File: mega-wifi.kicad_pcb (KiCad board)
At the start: 2 copper layers, 83.8 x 51 mm, 51 parts, among them P1 NP, P2 MD-CART-FINGERS, Q1 2N7002, U1 SC16C550BIB48, U2 S29GL032N, U3 ESP-12E, U4 AZ1117CH-3.3, U5 74LVC1G08GW, U6 74LVC162245, U7 74LVC245, U8 74LVC162245, Y1 24 MHz

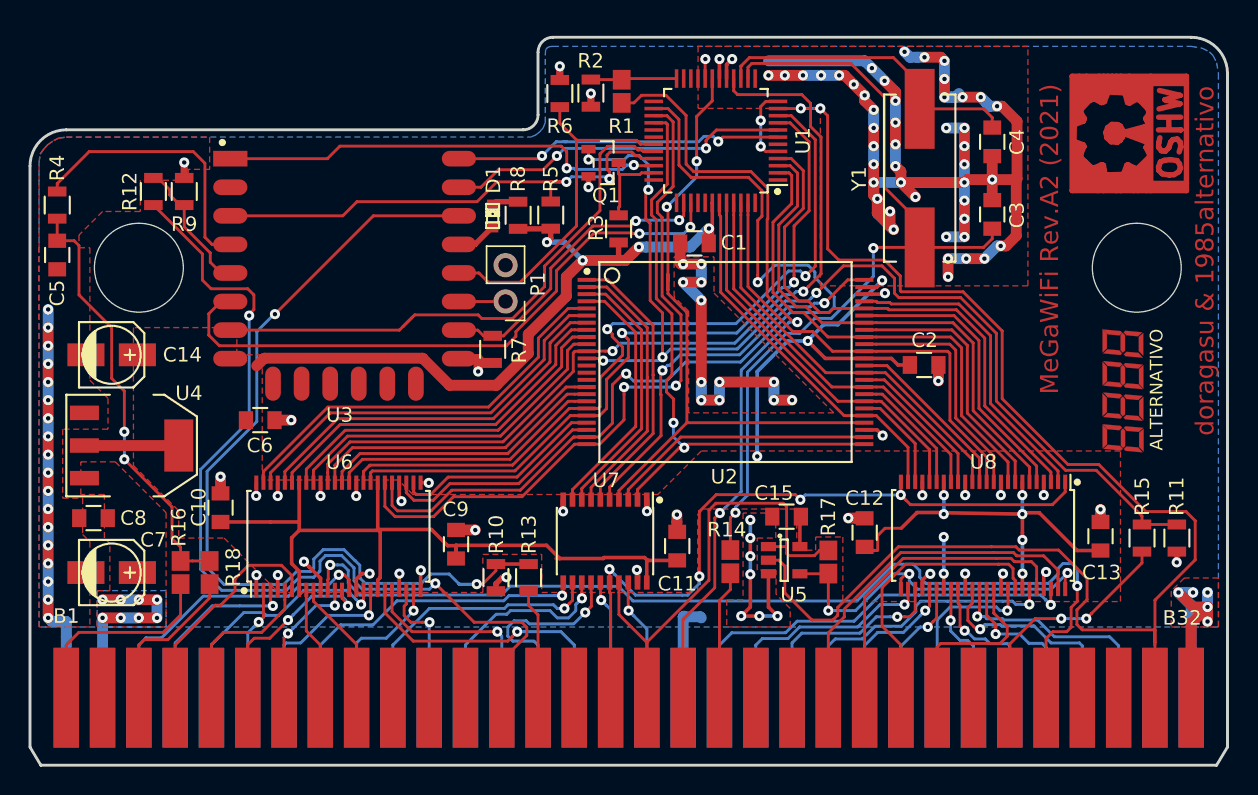
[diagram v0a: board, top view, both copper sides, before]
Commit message: Rev.B PCB
* Replace obsolete SC16C550BIB48 with SC16C550BIBS
* Replace ESP8266 with ESP32-C3
* Implement 64 Mbit hack
* Add USB-C debug header for ESP32-C3
* Many PCB improvements
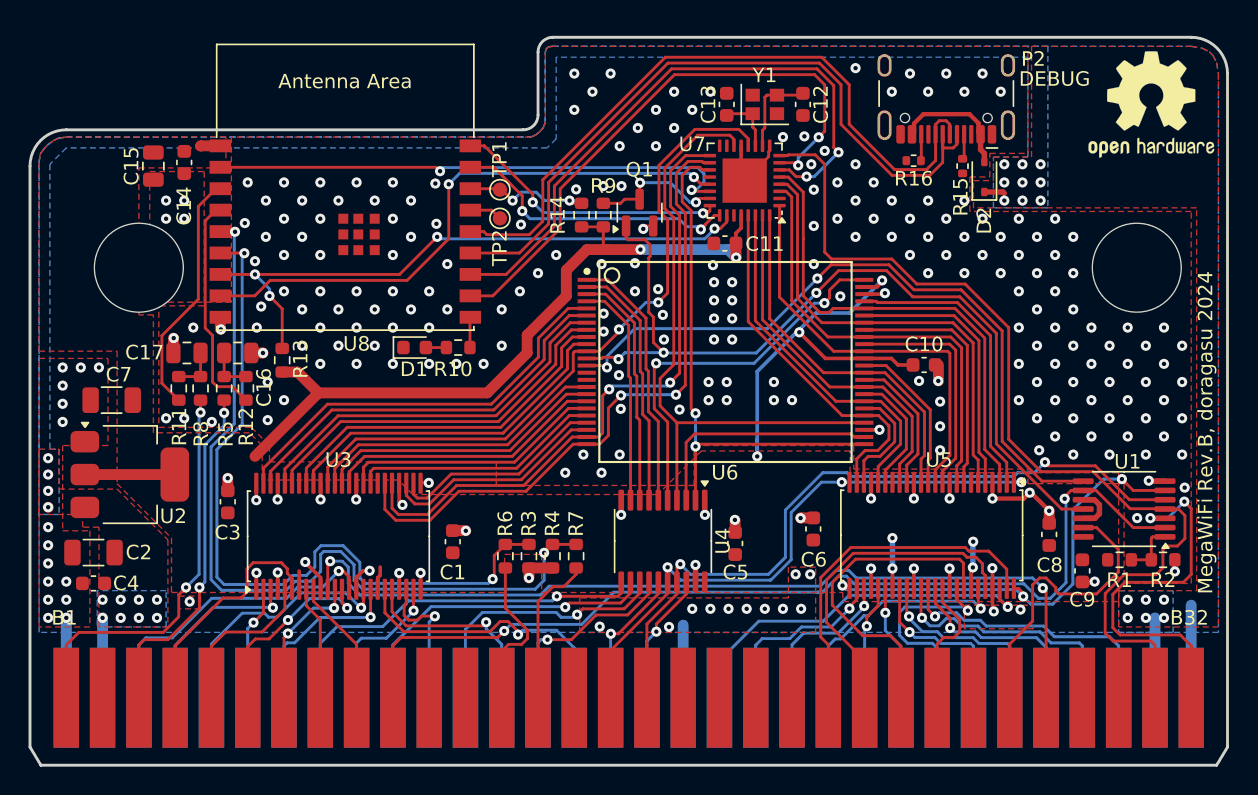
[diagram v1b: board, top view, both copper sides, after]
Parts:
- removed the C5 at (106.0, 95.2)
- removed the P1 at (137.4, 98.5)
- removed R17, R18: NP, doragasu:JUMPER_0805
- removed the R4 at (106.0, 91.8)
- removed the R6 at (141.2, 83.9)
- removed the R7 at (136.5, 101.9)
- removed the REF** at (180.6, 104.8)
- removed the REF** at (182.2, 83.8)
- removed Symbol_OSHW-Logo_CopperTop_Negative: VAL**, Symbols:Symbol_OSHW-Logo_CopperTop_Negative
- removed the U3 at (118.2, 88.5)
- removed the U5 at (156.9, 116.6)
- added C15: 10u, Capacitor_SMD:C_0805_2012Metric, F.Cu at (112.8, 89.0)
- added C16: 1u, Capacitor_SMD:C_0805_2012Metric, F.Cu at (118.7, 102.1)
- added C17: 1u, Capacitor_SMD:C_0805_2012Metric, F.Cu at (115.1, 102.1)
- added D2: 1N5819WS, Diode_SMD:D_SOD-323, F.Cu at (170.9, 89.8)
- added P2: USB_C_Receptacle_USB2.0_16P, Connector_USB:USB_C_Receptacle_HCTL_HC-TYPE-C-16P-01A, F.Cu at (168.3, 83.1)
- added R12: 2k2, Resistor_SMD:R_0603_1608Metric, F.Cu at (119.3, 104.6)
- added R13: 10k, Resistor_SMD:R_0603_1608Metric, F.Cu at (121.8, 102.6)
- added R8: 8k2, Resistor_SMD:R_0603_1608Metric, F.Cu at (116.1, 104.6)
- added REF**: OSHW-Logo2_9.8x8mm_SilkScreen, Symbol:OSHW-Logo2_9.8x8mm_SilkScreen, F.Cu at (182.6, 84.7)
- added TP1: TestPoint, TestPoint:TestPoint_Pad_D1.0mm, F.Cu at (137.0, 90.7)
- added TP2: TestPoint, TestPoint:TestPoint_Pad_D1.0mm, F.Cu at (137.0, 92.7)
- added U7: SC16C550BIBS, Package_DFN_QFN:HVQFN-32-1EP_5x5mm_P0.5mm_EP3.1x3.1mm, F.Cu at (154.2, 90.0)
- added U8: ESP32-C3-WROOM-02, PCM_Espressif:ESP32-C3-WROOM-02, F.Cu at (126.2, 93.5)
- C1: renamed from C9; footprint Capacitors_SMD:C_0805 -> Capacitor_SMD:C_0603_1608Metric
- C10: renamed from C2; footprint Capacitors_SMD:C_0805 -> Capacitor_SMD:C_0603_1608Metric
- C11: renamed from C1; footprint Capacitors_SMD:C_0805 -> Capacitor_SMD:C_0603_1608Metric
- C12: renamed from C3; value 22p -> 12p; footprint Capacitors_SMD:C_0805 -> Capacitor_SMD:C_0603_1608Metric
- C13: renamed from C4; value 22p -> 12p; footprint Capacitors_SMD:C_0805 -> Capacitor_SMD:C_0603_1608Metric
- C14: renamed from C6; footprint Capacitors_SMD:C_0805 -> Capacitor_SMD:C_0603_1608Metric
- C2: renamed from C7; value 22u_6.3V -> 22u; footprint Capacitors_SMD:c_elec_4x4.5 -> Capacitor_SMD:C_1206_3216Metric
- C3: renamed from C10; footprint Capacitors_SMD:C_0805 -> Capacitor_SMD:C_0603_1608Metric
- C4: renamed from C8; footprint Capacitors_SMD:C_0805 -> Capacitor_SMD:C_0603_1608Metric
- C5: renamed from C11; footprint Capacitors_SMD:C_0805 -> Capacitor_SMD:C_0603_1608Metric
- C6: renamed from C12; footprint Capacitors_SMD:C_0805 -> Capacitor_SMD:C_0603_1608Metric
- C7: renamed from C14; value 22u_6.3V -> 22u; footprint Capacitors_SMD:c_elec_4x4.5 -> Capacitor_SMD:C_1206_3216Metric
- C8: renamed from C13; footprint Capacitors_SMD:C_0805 -> Capacitor_SMD:C_0603_1608Metric
- C9: renamed from C15; footprint Capacitors_SMD:C_0805 -> Capacitor_SMD:C_0603_1608Metric
- D1: value NP -> KT-0603R; footprint LEDs:LED-0603 -> LED_SMD:LED_0603_1608Metric
- Q1: footprint Transistors_SMD:sot23 -> Package_TO_SOT_SMD:SOT-23
- R1: value 0 -> 10k; footprint doragasu:JUMPER_0805 -> Resistor_SMD:R_0603_1608Metric
- R10: renamed from R8; value NP -> 220; footprint Resistors_SMD:R_0805 -> Resistor_SMD:R_0603_1608Metric
- R11: value 100k -> 2k2; footprint Resistors_SMD:R_0805 -> Resistor_SMD:R_0603_1608Metric
- R14: value NP -> 10k; footprint doragasu:JUMPER_0805 -> Resistor_SMD:R_0603_1608Metric
- R15: value 47k -> 5k1; footprint Resistors_SMD:R_0805 -> Resistor_SMD:R_0402_1005Metric
- R16: value NP -> 5k1; footprint doragasu:JUMPER_0805 -> Resistor_SMD:R_0402_1005Metric
- R2: footprint Resistors_SMD:R_0805 -> Resistor_SMD:R_0603_1608Metric
- R3: renamed from R9; footprint Resistors_SMD:R_0805 -> Resistor_SMD:R_0603_1608Metric
- R4: renamed from R10; footprint Resistors_SMD:R_0805 -> Resistor_SMD:R_0603_1608Metric
- R5: value 10k -> 8k2; footprint Resistors_SMD:R_0805 -> Resistor_SMD:R_0603_1608Metric
- R6: renamed from R12; footprint Resistors_SMD:R_0805 -> Resistor_SMD:R_0603_1608Metric
- R7: renamed from R13; footprint Resistors_SMD:R_0805 -> Resistor_SMD:R_0603_1608Metric
- R9: renamed from R3; footprint Resistors_SMD:R_0805 -> Resistor_SMD:R_0603_1608Metric
- U1: value SC16C550BIB48 -> 74LVC08; footprint Housings_QFP:TQFP-48_7x7mm_Pitch0.5mm -> Package_SO:TSSOP-14_4.4x5mm_P0.65mm
- U2: renamed from U4; value AZ1117CH-3.3 -> AMS1117-3.3; footprint SMD_Packages:SOT-223 -> Package_TO_SOT_SMD:SOT-223
- U3: renamed from U6; value 74LVC162245 -> 74LVC16245; footprint Housings_SSOP:TSSOP-48_6.1x12.5mm_Pitch0.5mm -> Package_SO:TSSOP-48_6.1x12.5mm_P0.5mm
- U4: renamed from U7; footprint Housings_SSOP:SSOP-20_4.4x6.5mm_Pitch0.65mm -> Package_SO:TSSOP-20_4.4x6.5mm_P0.65mm
- U5: renamed from U8; value 74LVC162245 -> 74LVC16245; footprint Housings_SSOP:TSSOP-48_6.1x12.5mm_Pitch0.5mm -> Package_SO:TSSOP-48_6.1x12.5mm_P0.5mm
- U6: renamed from U2; value S29GL032N -> S29GL064N
- Y1: footprint Crystals:Crystal_HC49-SD_SMD -> Crystal:Crystal_SMD_2520-4Pin_2.5x2.0mm
- moved R11 70.6 mm to (114.6, 104.6), turned to -90 degrees
- moved R16 58.9 mm to (166.0, 88.6), turned to 180 degrees
- moved R2 51.7 mm to (183.5, 116.6), turned to 180 degrees
- moved R1 47.8 mm to (180.4, 116.6), turned to 180 degrees
- moved U1 38.5 mm to (180.7, 113.0)
- moved R6 35.5 mm to (137.4, 116.3)
- moved R3 35.1 mm to (139.1, 116.3), turned to 90 degrees
- moved R15 28.9 mm to (169.4, 89.0)
- moved R14 26.4 mm to (142.7, 92.5)
- moved R5 25.9 mm to (117.7, 104.6)
- moved C9 21.0 mm to (177.8, 117.4), turned to -90 degrees
- moved C14 18.8 mm to (114.9, 88.8), turned to -90 degrees
- moved C13 18.8 mm to (152.9, 84.7), turned to -90 degrees
- moved C12 15.3 mm to (158.2, 84.7), turned to 90 degrees
- moved Y1 12.0 mm to (155.6, 84.7), turned to 0 degrees
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- renumbered P2 to P1
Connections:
- net /#CE renamed /~{CE}
- net /#C_OE renamed /~{C_OE}
- net /#C_W renamed /~{C_W}
- C12 pad 2: /C_CLK -> Net-(U7-XTAL1)
- C13 pad 2: Net-(C4-Pad2) -> Net-(U7-XTAL2)
- D1 pad 1: Net-(D1-Pad1) -> GND
- D1 pad 2: Net-(D1-Pad2) -> Net-(D1-A)
- P1 pad B1: Net-(P2-PadB1) -> Net-(P1-L_AUDIO)
- P1 pad B10: (no net) -> /C_A22
- P1 pad B11: (no net) -> unconnected-(P1-A23-PadB11)
- P1 pad B12: (no net) -> unconnected-(P1-VIDEO-PadB12)
- P1 pad B15: (no net) -> unconnected-(P1-HS_CLK-PadB15)
- P1 pad B17: /#C_CE -> /~{C_CE}
- P1 pad B18: /#C_AS -> unconnected-(P1-~{AS}-PadB18)
- P1 pad B19: Net-(P2-PadB19) -> unconnected-(P1-CLK-PadB19)
- P1 pad B2: (no net) -> unconnected-(P1-~{H_RESET}-PadB2)
- P1 pad B20: (no net) -> unconnected-(P1-~{DTACK}-PadB20)
- P1 pad B21: (no net) -> unconnected-(P1-~{CAS2}-PadB21)
- P1 pad B26: (no net) -> unconnected-(P1-~{LO_MEM}-PadB26)
- P1 pad B27: Net-(P2-PadB27) -> Net-(P1-~{RESET})
- P1 pad B29: (no net) -> unconnected-(P1-~{UDSW}-PadB29)
- P1 pad B3: Net-(P2-PadB3) -> Net-(P1-R_AUDIO)
- P1 pad B30: (no net) -> unconnected-(P1-~{S_RESET}-PadB30)
- P1 pad B31: /#C_TIME -> /~{C_TIME}
- P1 pad B32: GND -> Net-(P1-~{CART_IN})
- Q1 pad 1: /#RST -> /~{RST}
- Q1 pad 3: Net-(Q1-Pad3) -> Net-(Q1-D)
- R1 pad 2: /#C_AS -> VCC
- R10 pad 1: Net-(D1-Pad2) -> Net-(U8-GPIO10)
- R10 pad 2: VCC -> Net-(D1-A)
- R11 pad 1: GND -> /WiFi/PWM_L
- R11 pad 2: /#RST -> Net-(U8-GPIO4/ADC1_CH4)
- R14 pad 1: Net-(P2-PadB19) -> VCC
- R14 pad 2: /C_CLK -> Net-(U8-GPIO2/ADC1_CH2)
- R15 pad 1: /#RST -> Net-(P2-CC1)
- R15 pad 2: Net-(P2-PadB27) -> GND
- R16 pad 1: /WiFi/PWM -> Net-(P2-CC2)
- R16 pad 2: Net-(P2-PadB1) -> GND
- R2 pad 1: Net-(R1-Pad1) -> GND
- R2 pad 2: GND -> Net-(R1-Pad1)
- R5 pad 1: /WiFi/#W_PD -> /WiFi/PWM_R
- R5 pad 2: VCC -> Net-(P1-R_AUDIO)
- R9 pad 2: Net-(Q1-Pad3) -> Net-(Q1-D)
- U1 pad 1: (no net) -> Net-(R1-Pad1)
- U1 pad 10: /A7 -> VCC
- U1 pad 11: /#C_TIME -> /~{RST}
- U1 pad 12: Net-(U1-Pad12) -> VCC
- U1 pad 13: (no net) -> Net-(P1-~{RESET})
- U1 pad 14: /C_CLK -> VCC
- U1 pad 2: /D5 -> /C_A22
- U1 pad 3: /D6 -> Net-(P1-~{CART_IN})
- U1 pad 4: /D7 -> /~{C_TIME}
- U1 pad 5: Net-(U1-Pad12) -> /~{C_CE}
- U1 pad 6: (no net) -> /~{T_OE}
- U1 pad 7: /WiFi/W_TX -> GND
- U1 pad 8: /WiFi/W_RX -> /A22
- U1 pad 9: /A6 -> /C_A22
- U3 pad 38: /#W -> /~{W}
- U4 pad 17: /#C_CE -> /~{C_CE}
- U4 pad 4: /#OE -> /~{OE}
- U5 pad 25: /#T_OE -> /~{T_OE}
- U5 pad 48: /#T_OE -> /~{T_OE}
- U6 pad 11: /#W -> /~{W}
- U6 pad 12: /#RST -> /~{RST}
- U6 pad 13: (no net) -> /A22
- U6 pad 14: (no net) -> unconnected-(U6-~{WP}/ACC-Pad14)
- U6 pad 15: (no net) -> unconnected-(U6-RY/~{BY}-Pad15)
- U6 pad 28: /#OE -> /~{OE}
- Y1 pad 1: /C_CLK -> Net-(U7-XTAL2)
- Y1 pad 2: Net-(C4-Pad2) -> GND
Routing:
- net GND: track 238.5 -> 73.4 mm, vias 130 -> 277
- net /#C_TIME: track 102.1 -> 0.00 mm, vias 2 -> 0
- net /#RST: track 74.7 -> 0.00 mm, vias 5 -> 0
- net VCC: track 172.0 -> 100.5 mm, vias 15 -> 9
- net /C_A22: track 0.00 -> 68.5 mm, vias 0 -> 2
- net /~{C_TIME}: track 0.00 -> 66.9 mm
- net /#W: track 60.9 -> 0.00 mm, vias 2 -> 0
- net /~{RST}: track 0.00 -> 59.6 mm, vias 0 -> 3
- net /C_CLK: track 58.8 -> 0.00 mm, vias 2 -> 0
- net /#C_AS: track 55.5 -> 0.00 mm, vias 2 -> 0
- net Net-(P1-VSYNC): track 64.9 -> 11.0 mm, vias 2 -> 0
- net /~{C_CE}: track 0.00 -> 51.0 mm, vias 0 -> 2
- net /WiFi/USB_D-: track 0.00 -> 50.3 mm
- net /WiFi/USB_D+: track 0.00 -> 49.1 mm
- net /A22: track 0.00 -> 49.0 mm, vias 0 -> 2
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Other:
- board text added: "MegaWiFi Rev.B doragasu 2024"
- board text added: "MegaWiFi Rev.B, doragasu 2024"
- board text removed: "MeGaWiFi Rev.A2 (2021)"
- board text removed: "doragasu & 1985alternativo"
- board text removed: "doragasu (2021)"

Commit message: Fabrication tweaks
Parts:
- added REF**: Fiducial_0.5mm_Mask1.5mm, Fiducial:Fiducial_0.5mm_Mask1.5mm, F.Cu at (185.5, 82.3)
- added REF**: Fiducial_0.5mm_Mask1.5mm, Fiducial:Fiducial_0.5mm_Mask1.5mm, F.Cu at (112.6, 117.6)
- R1: value 10k -> 0R0
- R3, R4: value NP -> 10k
- R6, R7: value NP -> 5k6
- U6: footprint doragasu:TSOP48SP -> Package_SO:TSOP-I-48_18.4x12mm_P0.5mm
- moved REF** 3.05 mm to (182.6, 87.8)
- moved U6 0.09 mm to (152.8, 102.7), turned to 0 degrees
- turned R11 to 90 degrees
- turned R12 to 90 degrees
- turned R15 to 90 degrees
- turned R16 to 0 degrees
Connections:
- R1 pad 1: Net-(R1-Pad1) -> Net-(P1-~{CART_IN})
- R1 pad 2: VCC -> /C_A22
- R11 pad 1: /WiFi/PWM_L -> Net-(U8-GPIO4/ADC1_CH4)
- R11 pad 2: Net-(U8-GPIO4/ADC1_CH4) -> /WiFi/PWM_L
- R12 pad 1: /WiFi/PWM_R -> Net-(U8-GPIO5/ADC2_CH0)
- R12 pad 2: Net-(U8-GPIO5/ADC2_CH0) -> /WiFi/PWM_R
- R15 pad 1: Net-(P2-CC1) -> GND
- R15 pad 2: GND -> Net-(P2-CC1)
- R16 pad 1: Net-(P2-CC2) -> GND
- R16 pad 2: GND -> Net-(P2-CC2)
- R2 pad 2: Net-(R1-Pad1) -> Net-(P1-~{CART_IN})
- U1 pad 1: Net-(R1-Pad1) -> GND
- U1 pad 2: /C_A22 -> GND
- U1 pad 3: Net-(P1-~{CART_IN}) -> unconnected-(U1-Pad3)
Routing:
- net Net-(P1-~{CART_IN}): track 27.3 -> 16.3 mm, vias 2 -> 0
- net /~{C_TIME}: track 66.9 -> 62.6 mm
- net Net-(R1-Pad1): track 3.91 -> 0.00 mm
- net /C_A22: track 68.5 -> 67.7 mm
- net Net-(P1-~{RESET}): track 20.7 -> 19.9 mm

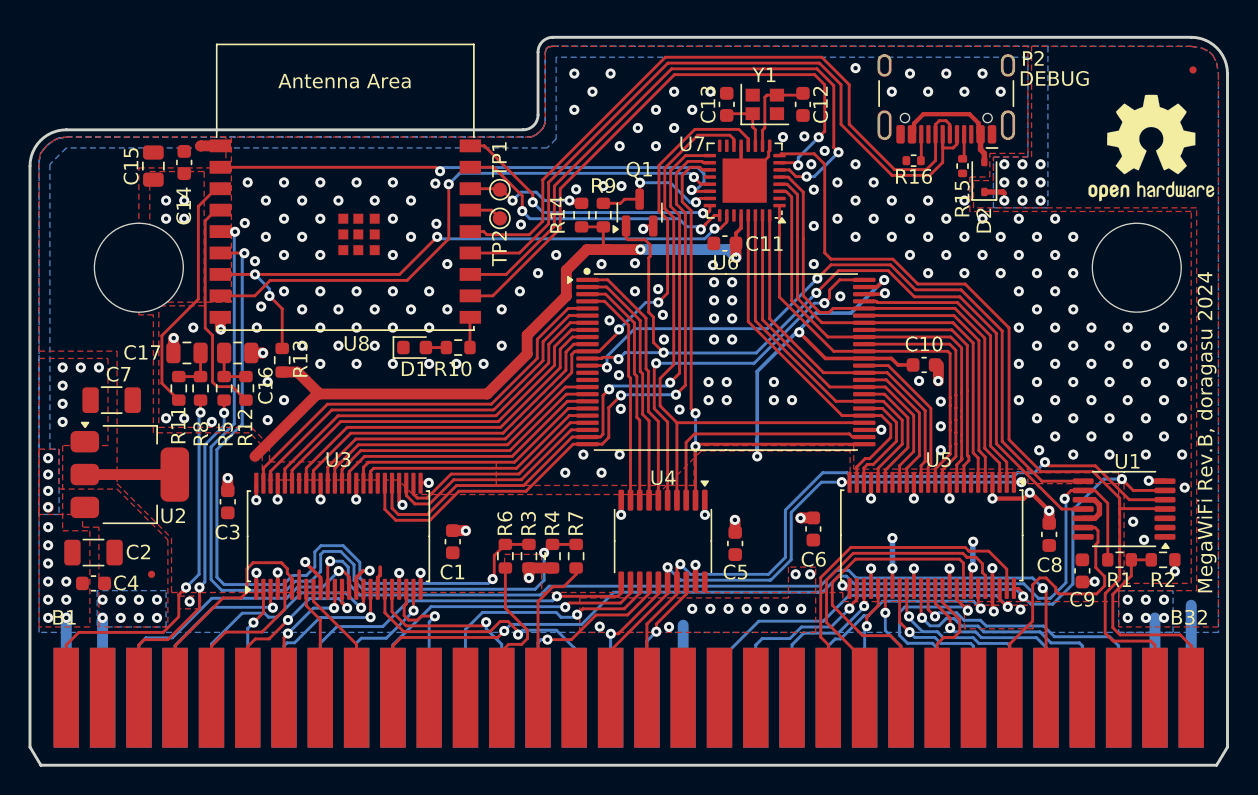
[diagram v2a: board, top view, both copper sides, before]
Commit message: Allow ESP32 to reset the host
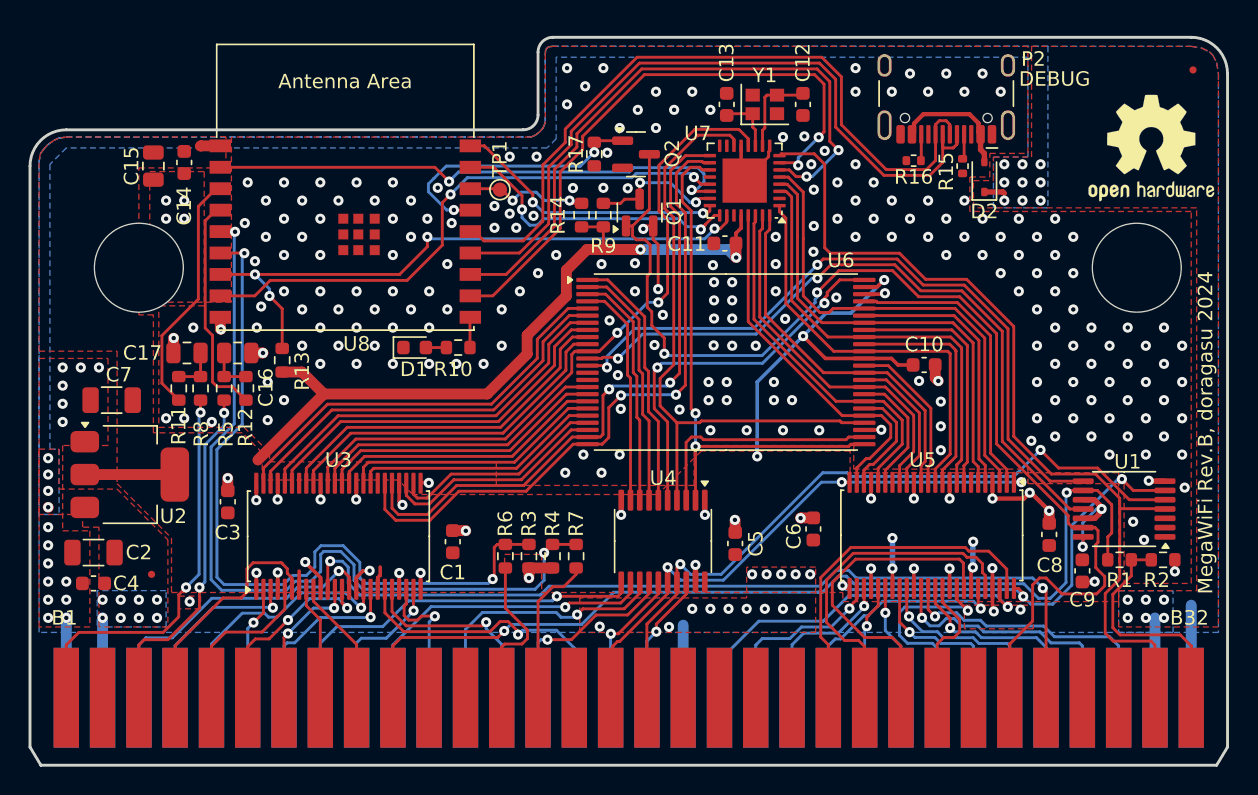
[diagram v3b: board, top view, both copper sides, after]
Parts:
- removed TP2: TestPoint, TestPoint:TestPoint_Pad_D1.0mm
- added Q2: 2N7002, Package_TO_SOT_SMD:SOT-23, F.Cu at (146.6, 88.2)
- added R17: 10k, Resistor_SMD:R_0603_1608Metric, F.Cu at (143.6, 88.2)
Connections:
- P1 pad B27: Net-(P1-~{RESET}) -> /~{C_RST}
- Q1 pad 1: /~{RST} -> /~{C_RST}
- U1 pad 13: Net-(P1-~{RESET}) -> /~{C_RST}
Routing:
- net /~{C_RST}: track 0.00 -> 80.6 mm, vias 0 -> 2
- net Net-(P1-~{RESET}): track 19.9 -> 0.00 mm
- net Net-(Q2-G): track 2.31 -> 19.3 mm, vias 0 -> 2
- net /~{RST}: track 59.6 -> 49.1 mm, vias 3 -> 2
- net VCC: track 100.9 -> 108.1 mm, vias 9 -> 11
- net GND: track 73.6 -> 78.2 mm, vias 277 -> 290
- net /WiFi/USB_D+: track 49.1 -> 50.9 mm
- net /~{C_OE}: track 41.8 -> 39.9 mm
- net /WiFi/USB_D-: track 50.3 -> 51.8 mm
- net /~{C_CE}: track 51.0 -> 49.8 mm
- net /WiFi/TX: track 40.9 -> 42.1 mm
- net /WiFi/RX: track 43.4 -> 44.5 mm
- net /C_A22: track 67.7 -> 68.5 mm
- net /WiFi/~{DSR}: track 20.3 -> 21.0 mm
- net /WiFi/~{DTR}: track 37.2 -> 37.8 mm
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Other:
- board text added: "30 degree beveled edge"
